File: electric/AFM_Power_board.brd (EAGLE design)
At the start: 63.2 x 55.9 mm, 16 parts, among them IC1 LM4041CILP, IC2 LM7805_TO220V, IC3 7812T, J2 694103303002

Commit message: allboards
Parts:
- removed C6: 1uF, BeagleBone_Black_Wireless:C050-024X044
- removed C7: 10uF, BeagleBone_Black_Wireless:C050-024X044
- removed IC2: LM7805_TO220V, IC_Power-Management:TO220V
- added C10, C12: 1uF, BeagleBone_Black_Wireless:C050-024X044
- added C11, C9: 10uF, BeagleBone_Black_Wireless:C050-024X044
- added C8: 220uF, BeagleBone_Blue_R3:E5-8,5
- added D2, D3, D5, D6: 1n4004, diode:SOD123
- added J3: 694103303002, DC Power Jacks:694103303002
- added L1: 60Ohm@100 MHz, Wurth_EMC Components_WE-CBF:WE-CBF_0603_W2.2
- added R2: (no value), BeagleBone_Black_Wireless:0204/5
- added U1: LM7905CT/NOPB, LM7905CT_NOPB:TO254P1016X4575X1955-3
- added VR1: LM7805MP/NOPB, LM7805MP_NOPB:VREG_LM7805MP/NOPB
- IC3: value 7812T -> LM4041CILP; device adafruit:TO220H -> texas:LP_O-PBCY-W3
- moved IC3 26.7 mm to (20.3, 41.9), turned to 180 degrees
- moved C4 20.5 mm to (2.54, 31.8), turned to 270 degrees
- moved C1 18.9 mm to (36.8, 24.1)
- moved C2 17.0 mm to (30.5, 25.4)
- moved C3 17.0 mm to (25.4, 25.4)
- moved L3 14.8 mm to (21.6, 27.9)
- moved L4 13.0 mm to (21.6, 17.8)
- moved J2 12.7 mm to (57.1, 40.6), turned to 90 degrees
- moved C5 12.5 mm to (7.62, 31.8), turned to 270 degrees
- moved R1 10.2 mm to (26.7, 35.6)
- moved IC1 5.68 mm to (36.8, 35.6)
- moved B1 2.84 mm to (34.3, 26.7)
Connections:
- removed net N$3: IC3.1, L3.2
- removed net V12_OUT: C4.1, C5.1, IC2.1, IC3.3, J1.3
- new net GROUND: C1.-, C10.1, C2.2, C3.2, C8.+, C9.1, J2.2, J2.3, J3.2, J3.3, L4.1
- new net N$10: C10.2, C8.-, C9.2, D2.A, D6.A, L1.1
- new net N$11: C1.+, C2.1, C3.1, D3.C, D5.C, L3.1
- new net N$8: IC3.3, R2.2
- new net N$9: D5.A, D6.C, J3.1
- new net POWERP: D2.C, D3.A, J2.1
- new net VMINUS5_OUT: C11.2, C12.2, J1.3, R2.1, U1.3
- net AGND: now also B1.GND@0, B1.GND@1, B1.GND@2, C11.1, C12.1, U1.1, VR1.2, VR1.4; no longer C6.2, C7.2, IC2.2
- net N$1: now also L3.2, VR1.1; no longer C1.+, C2.1, C3.1, J2.1, L3.1
- net N$2: now also L1.2, U1.2; no longer B1.GND@2, C1.-, C2.2, C3.2, J2.2, J2.3, L4.1
- net V5_OUT: now also C4.1, C5.1, VR1.3; no longer C6.1, C7.1, IC2.3
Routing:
- net VMINUS5_OUT: track 0.00 -> 116.3 mm, vias 0 -> 2
- net V12_OUT: track 89.9 -> 0.00 mm
- net GROUND: track 0.00 -> 84.3 mm, vias 0 -> 2
- net N$11: track 0.00 -> 54.9 mm, vias 0 -> 2
- net N$2: track 61.4 -> 7.47 mm
- net N$10: track 0.00 -> 38.0 mm
- net N$1: track 28.3 -> 4.74 mm
- net N$9: track 0.00 -> 23.4 mm
- net POWERP: track 0.00 -> 16.2 mm
- net N$3: track 12.0 -> 0.00 mm
- net N$8: track 0.00 -> 5.61 mm
- net N$4: track 12.3 -> 11.2 mm
- net V5_OUT: track 64.2 -> 64.8 mm

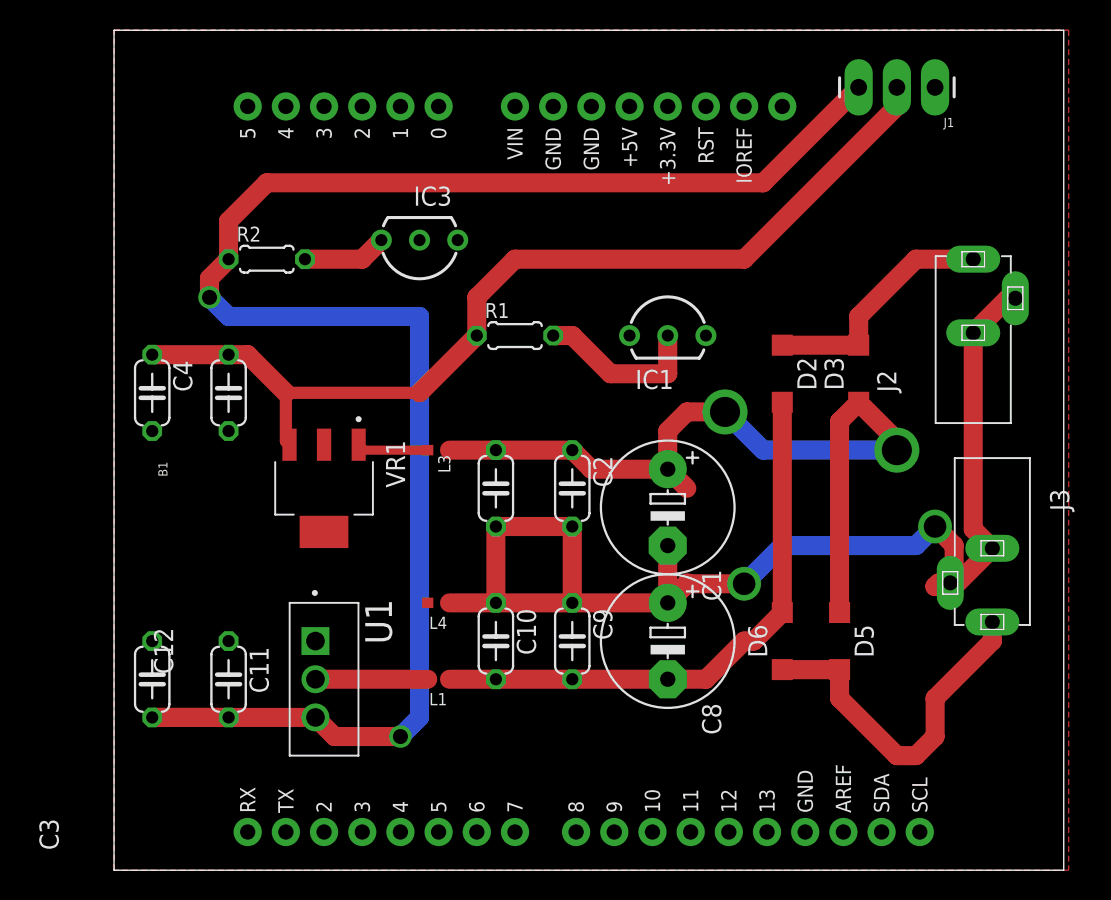
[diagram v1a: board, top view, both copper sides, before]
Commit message: movied power lines to right position
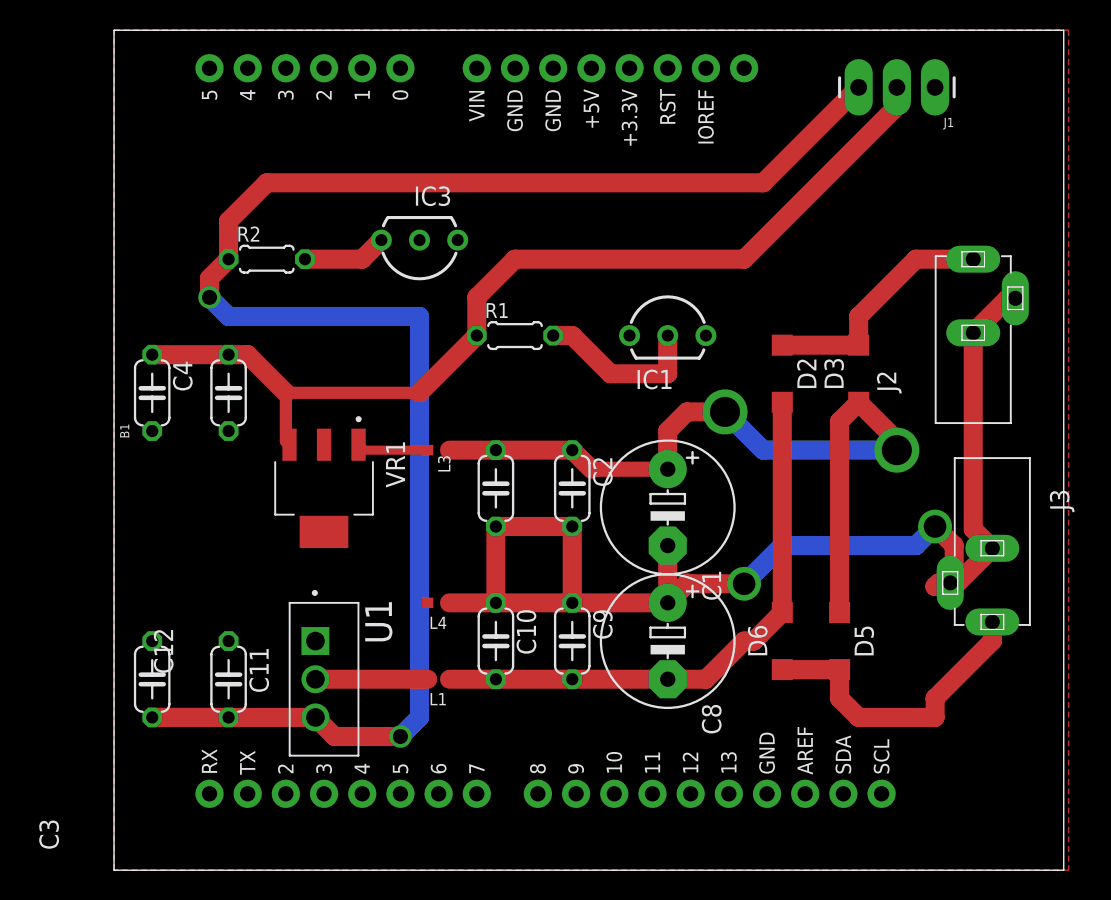
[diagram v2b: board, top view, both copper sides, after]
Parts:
- moved B1 3.59 mm to (31.8, 29.2)
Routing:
- net N$9: track 23.4 -> 20.5 mm
- net N$11: track 54.9 -> 53.1 mm
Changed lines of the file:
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@@
 <attribute name="Z-MAX" value="110Ohm@650 MHz" x="21.59" y="17.78" size="1.778" layer="27" rot="R180" display="off"/>
 </element>
-<element name="B1" library="SparkFun-Boards" library_urn="urn:adsk.eagle:library:509" package="UNO_R3_SHIELD" package3d_urn="urn:adsk.eagle:package:41384914/1" value="ARDUINO_UNO_R3_SHIELDBASIC" x="34.29" y="26.67" smashed="yes" rot="R90">
-<attribute name="NAME" x="3.556" y="26.67" size="0.6096" layer="25" font="vector" ratio="20" rot="R90" align="bottom-center"/>
-<attribute name="VALUE" x="64.008" y="26.67" size="0.6096" layer="27" font="vector" ratio="20" rot="R90" align="top-center"/>
+<element name="B1" library="SparkFun-Boards" library_urn="urn:adsk.eagle:library:509" package="UNO_R3_SHIELD" package3d_urn="urn:adsk.eagle:package:41384914/1" value="ARDUINO_UNO_R3_SHIELDBASIC" x="31.75" y="29.21" smashed="yes" rot="R90">
+<attribute name="NAME" x="1.016" y="29.21" size="0.6096" layer="25" font="vector" ratio="20" rot="R90" align="bottom-center"/>
+<attribute name="VALUE" x="58.928" y="31.75" size="0.6096" layer="27" font="vector" ratio="20" rot="R90" align="top-center"/>
 </element>
 <element name="J1" library="SparkFun-Connectors" library_urn="urn:adsk.eagle:library:513" package="1X03_LONGPADS" package3d_urn="urn:adsk.eagle:package:38068/2" value="" x="54.61" y="52.07" smashed="yes" rot="R180">
@@
 <wire x1="58.42" y1="16.51" x2="58.42" y2="15.24" width="1.27" layer="1"/>
 <wire x1="58.42" y1="15.24" x2="54.61" y2="11.43" width="1.27" layer="1"/>
-<wire x1="54.61" y1="11.43" x2="54.61" y2="8.89" width="1.27" layer="1"/>
-<wire x1="54.61" y1="8.89" x2="53.34" y2="7.62" width="1.27" layer="1"/>
+<wire x1="54.61" y1="11.43" x2="54.61" y2="10.16" width="1.27" layer="1"/>
 <contactref element="D5" pad="A"/>
 <contactref element="D6" pad="C"/>
-<wire x1="53.34" y1="7.62" x2="52.07" y2="7.62" width="1.27" layer="1"/>
-<wire x1="52.07" y1="7.62" x2="48.26" y2="11.43" width="1.27" layer="1"/>
+<wire x1="54.61" y1="10.16" x2="49.53" y2="10.16" width="1.27" layer="1"/>
+<wire x1="49.53" y1="10.16" x2="48.26" y2="11.43" width="1.27" layer="1"/>
 <wire x1="48.26" y1="11.43" x2="48.26" y2="13.34" width="1.27" layer="1"/>
 <wire x1="44.45" y1="13.34" x2="48.26" y2="13.34" width="1.27" layer="1"/>
@@
 <contactref element="L3" pad="1"/>
 <wire x1="36.83" y1="26.67" x2="36.83" y2="29.21" width="1.27" layer="1"/>
-<wire x1="36.83" y1="26.67" x2="31.75" y2="26.67" width="1.27" layer="1"/>
 <wire x1="31.75" y1="26.67" x2="30.48" y2="27.94" width="1.27" layer="1"/>
 <wire x1="30.48" y1="27.94" x2="25.4" y2="27.94" width="1.27" layer="1"/>
-<wire x1="38.1" y1="25.4" x2="36.83" y2="26.67" width="1.27" layer="1"/>
 <wire x1="25.4" y1="27.94" x2="22.315" y2="27.94" width="1.27" layer="1"/>
 <contactref element="D3" pad="C"/>
@@
 <wire x1="52.07" y1="27.94" x2="43.18" y2="27.94" width="1.27" layer="16"/>
 <wire x1="43.18" y1="27.94" x2="40.64" y2="30.48" width="1.27" layer="16"/>
+<wire x1="36.83" y1="26.67" x2="31.75" y2="26.67" width="1.016" layer="1"/>
 </signal>
 <signal name="POWERP">
